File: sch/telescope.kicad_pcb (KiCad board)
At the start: 2 copper layers, 64 parts, among them J1 USB_B, J2 M1, J3 M2, J4 12V, Q1 MMBT3904, Q2 MMBT3904, Q3 MMBT3904, SW1 RST, SW2 IO0, SW3 PWR, U1 A5984GLPTR-T, U2 A5984GLPTR-T, U3 FT260S-U, U5 ESP32-WROOM-32, U6 INA180A1, U7 AP62200WU-7

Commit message: layout, route, and add digikey numbers
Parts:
- added H1: MountingHole_Pad, MountingHole:MountingHole_3.2mm_M3_Pad, F.Cu at (184.0, 85.0)
- added H2: MountingHole_Pad, MountingHole:MountingHole_3.2mm_M3_Pad, F.Cu at (231.0, 127.0)
- added H3: MountingHole_Pad, MountingHole:MountingHole_3.2mm_M3_Pad, F.Cu at (206.0, 149.0)
- added J5: UART, Connector_PinHeader_2.54mm:PinHeader_1x04_P2.54mm_Vertical, F.Cu at (210.4, 112.0)
- added REF**: Ade, Logo:Ade, F.Cu at (224.6, 100.6)
- C13, C15, C16, C17, C18, C19, C2, C3, C4, C5, D1, D2, D3, L1, Q2, Q3, R10, R14, R18, R19, R20, R21, R22, R24, R25, R8, R9, U1, U2, U6, U7: moved to B.Cu
- J2, J3: footprint Connector_JST:JST_PH_B4B-PH-K_1x04_P2.00mm_Vertical -> Connector_JST:JST_PH_S4B-PH-K_1x04_P2.00mm_Horizontal
- R23: footprint Resistor_SMD:R_2512_6332Metric_Pad1.40x3.35mm_HandSolder -> Resistor_SMD:R_1206_3216Metric_Pad1.30x1.75mm_HandSolder; moved to B.Cu
- R3, R4, R6, R7: footprint Resistor_SMD:R_0805_2012Metric_Pad1.20x1.40mm_HandSolder -> Resistor_SMD:R_1206_3216Metric_Pad1.30x1.75mm_HandSolder; moved to B.Cu
- SW1, SW2: footprint Button_Switch_SMD:SW_Push_1P1T_NO_6x6mm_H9.5mm -> TS04-66-43-BK-160:SW_TS04-66-43-BK-160-SMT
- moved D1 135.9 mm to (228.5, 141.6), turned to 180 degrees
- moved D2 123.7 mm to (216.5, 142.1)
- moved D3 122.5 mm to (216.5, 139.6)
- moved JP2 118.0 mm to (219.0, 118.0), turned to 90 degrees
- moved C7 117.0 mm to (227.0, 123.0), turned to 90 degrees
- moved C14 114.9 mm to (232.0, 102.8), turned to 180 degrees
- moved C6 114.7 mm to (224.0, 123.0), turned to 90 degrees
- moved JP1 114.2 mm to (215.0, 118.1), turned to 90 degrees
- moved R1 109.4 mm to (227.0, 131.3), turned to 90 degrees
- moved C16 106.2 mm to (218.8, 128.2), turned to 90 degrees
- moved R5 102.4 mm to (224.0, 131.3), turned to 90 degrees
- moved C13 100.9 mm to (217.6, 86.8), turned to -90 degrees
- moved L1 99.8 mm to (219.5, 121.3), turned to 90 degrees
- moved R2 98.7 mm to (214.0, 136.5), turned to 180 degrees
- moved R14 97.5 mm to (231.5, 105.5), turned to 90 degrees
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- renumbered R16 to R26
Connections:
- JP1 pad 1: /ESP_TX -> Net-(JP1-A)
- JP1 pad 2: Net-(JP1-B) -> /ESP_TX
- U1 pad 15: Net-(J2-Pin_2) -> Net-(J2-Pin_3)
- U1 pad 18: Net-(J2-Pin_1) -> Net-(J2-Pin_4)
- U1 pad 19: Net-(J2-Pin_3) -> Net-(J2-Pin_2)
- U1 pad 22: Net-(J2-Pin_4) -> Net-(J2-Pin_1)
- U2 pad 15: Net-(J3-Pin_2) -> Net-(J3-Pin_3)
- U2 pad 18: Net-(J3-Pin_1) -> Net-(J3-Pin_4)
- U2 pad 19: Net-(J3-Pin_3) -> Net-(J3-Pin_2)
- U2 pad 22: Net-(J3-Pin_4) -> Net-(J3-Pin_1)
- U3 pad 14: Net-(JP1-B) -> Net-(JP1-A)
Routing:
- net +3V3: track 0.00 -> 203.8 mm, vias 0 -> 9
- net +12V: track 0.00 -> 107.0 mm, vias 0 -> 6
- net /~{M_ENA}: track 0.00 -> 85.7 mm, vias 0 -> 1
- net /ESP_EN: track 0.00 -> 60.2 mm, vias 0 -> 1
- net /M_SLEEP: track 0.00 -> 58.5 mm, vias 0 -> 1
- net /ISENSE: track 0.00 -> 54.5 mm, vias 0 -> 1
- net /ESP_TX: track 0.00 -> 47.3 mm
- net /ESP_IO0: track 0.00 -> 46.2 mm, vias 0 -> 2
- net /VSENSE: track 0.00 -> 44.5 mm, vias 0 -> 1
- net /ESP_RX: track 0.00 -> 44.4 mm
- net /M1_MS1: track 0.00 -> 43.9 mm, vias 0 -> 1
- net /~{M_RST}: track 0.00 -> 41.3 mm, vias 0 -> 2
- net /M1_MS3: track 0.00 -> 39.7 mm, vias 0 -> 1
- net /FT_RTS: track 0.00 -> 39.6 mm, vias 0 -> 1
- net /M2_STEP: track 0.00 -> 35.6 mm, vias 0 -> 1
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- added copper zone on B.Cu, net GND
- added copper zone on F.Cu, net GND
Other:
- board outline added: 56.2 x 77 mm
- board text added: "JLCJLCJLCJLC"
- board text added: "by Rio"

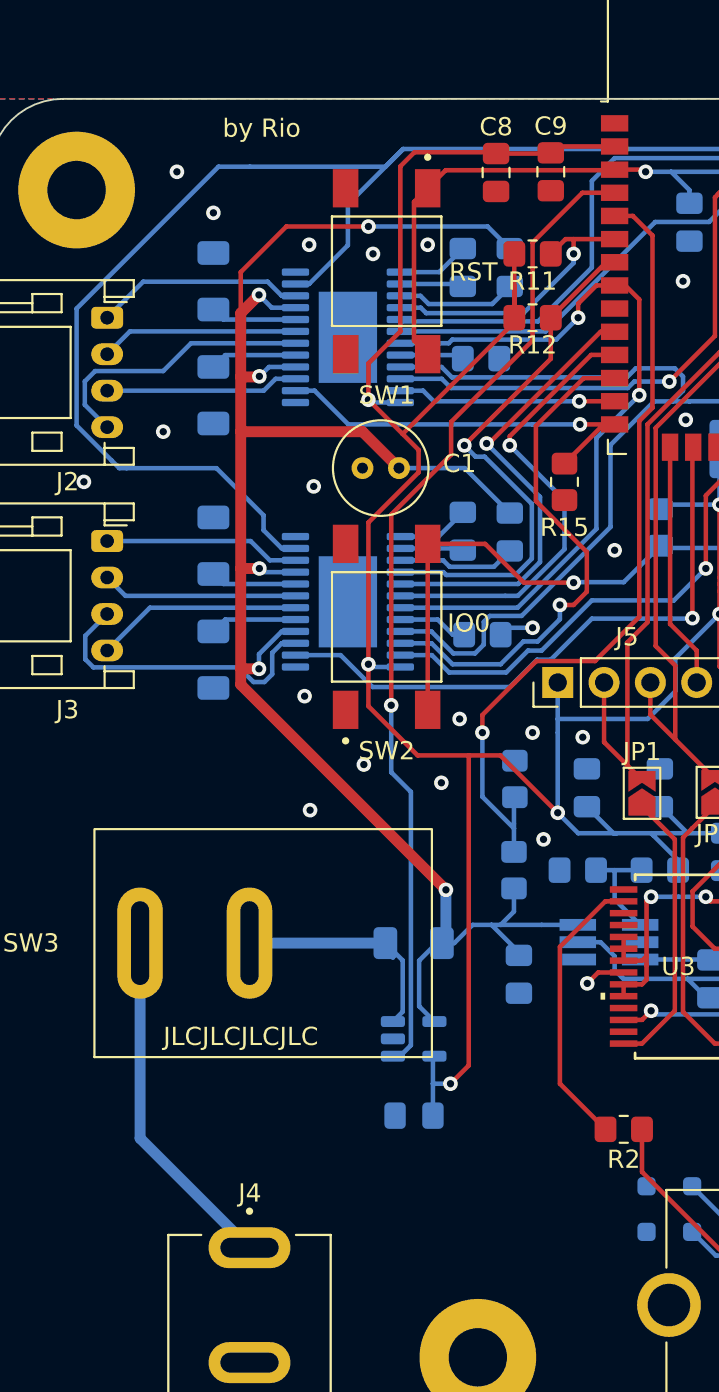
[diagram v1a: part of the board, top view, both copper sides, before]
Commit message: add some more silkscreen
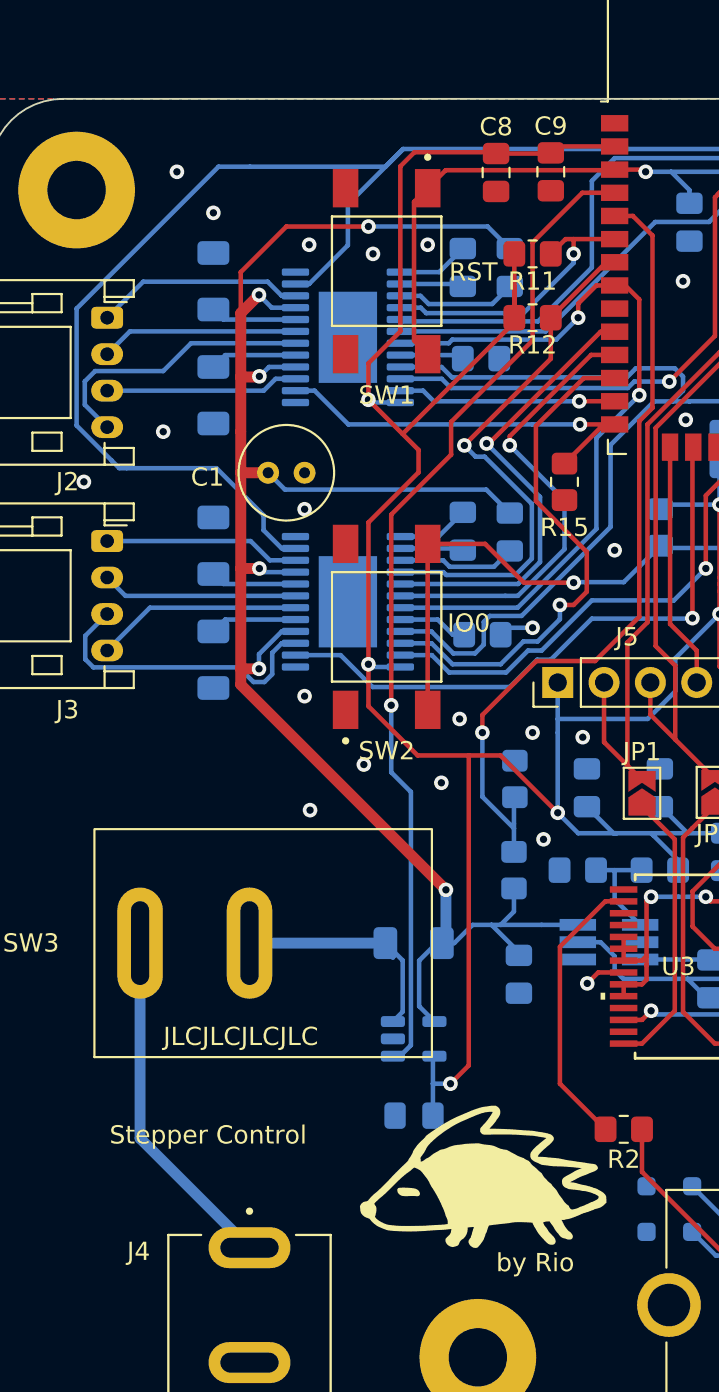
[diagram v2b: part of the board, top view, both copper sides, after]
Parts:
- added G***: LOGO, LOGO, F.Cu at (206.2, 139.4)
- added G***: LOGO, LOGO, B.Cu at (226.4, 92.8)
- added G***: LOGO, LOGO, B.Cu at (191.8, 135.0)
- moved C1 7.18 mm to (194.5, 100.5), turned to 0 degrees
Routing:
- net +12V: track 107.0 -> 106.1 mm
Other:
- board text added: "Stepper Control"
